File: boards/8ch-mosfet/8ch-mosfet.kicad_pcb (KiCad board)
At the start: 2 copper layers, 184.5 x 137 mm, 153 parts, among them J1 N2K, J10 Screw_Terminal_01x02, J11 Screw_Terminal_01x02, J12 Screw_Terminal_01x02, J2 I2C, J3 Screw_Terminal_01x08, J5 Screw_Terminal_01x02, J6 Screw_Terminal_01x02, J7 Screw_Terminal_01x02, J8 Screw_Terminal_01x02, J9 Screw_Terminal_01x02, M1 Fan_4pin, M2 Fan_4pin, Q1 2N7002, Q10 IRF4905, Q11 2N7002, Q12 IRF4905, Q13 2N7002, Q14 IRF4905, Q15 2N7002, Q16 IRF4905, Q2 IRF4905, Q3 2N7002, Q4 IRF4905, Q5 2N7002, Q6 IRF4905, Q7 2N7002, Q8 IRF4905, Q9 2N7002, U1 ESP32-DEVKITC, U10 ACS725xLCTR-20AU, U11 ACS725xLCTR-20AU, U12 ACS725xLCTR-20AU, U13 MCP1502, U2 MCP3208, U3 R-78K5.0-1.0, U4 MCP3221A0T, U5 ACS725xLCTR-20AU, U6 ACS725xLCTR-20AU, U7 ACS725xLCTR-20AU, U8 ACS725xLCTR-20AU, U9 ACS725xLCTR-20AU

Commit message: more routing and layout
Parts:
- removed J1: N2K, Connector_PinHeader_2.54mm:PinHeader_1x04_P2.54mm_Vertical
- removed J2: I2C, Connector_PinHeader_2.54mm:PinHeader_1x04_P2.54mm_Vertical
- removed R40: 2.2K, Resistor_SMD:R_0805_2012Metric_Pad1.20x1.40mm_HandSolder
- added C31: 33pF, Capacitor_SMD:C_0805_2012Metric_Pad1.18x1.45mm_HandSolder, F.Cu at (-56.4, -0.26)
- added C32: 33pF, Capacitor_SMD:C_0805_2012Metric_Pad1.18x1.45mm_HandSolder, F.Cu at (-63.3, -0.26)
- added C33: 33pF, Capacitor_SMD:C_0805_2012Metric_Pad1.18x1.45mm_HandSolder, F.Cu at (-56.4, 4.32)
- added C34: 33pF, Capacitor_SMD:C_0805_2012Metric_Pad1.18x1.45mm_HandSolder, F.Cu at (-63.2, 4.32)
- added C35: 10uF, Capacitor_SMD:C_0805_2012Metric_Pad1.18x1.45mm_HandSolder, F.Cu at (-56.4, 8.91)
- added C36: 10uF, Capacitor_SMD:C_0805_2012Metric_Pad1.18x1.45mm_HandSolder, F.Cu at (-54.1, 8.89)
- added C37: 33pF, Capacitor_SMD:C_0805_2012Metric_Pad1.18x1.45mm_HandSolder, F.Cu at (-16.6, 7.17)
- added C38: 33pF, Capacitor_SMD:C_0805_2012Metric_Pad1.18x1.45mm_HandSolder, F.Cu at (-16.6, 10.2)
- added C39: 10uF, Capacitor_SMD:C_0805_2012Metric_Pad1.18x1.45mm_HandSolder, F.Cu at (-21.6, 26.4)
- added C40: 33pF, Capacitor_SMD:C_0805_2012Metric_Pad1.18x1.45mm_HandSolder, F.Cu at (-11.8, 4.32)
- added C41: 33pF, Capacitor_SMD:C_0805_2012Metric_Pad1.18x1.45mm_HandSolder, F.Cu at (-11.8, 7.17)
- added C42: 10uF, Capacitor_SMD:C_0805_2012Metric_Pad1.18x1.45mm_HandSolder, F.Cu at (-11.2, -0.76)
- added C43: 1uF/50v, Capacitor_SMD:C_0805_2012Metric_Pad1.18x1.45mm_HandSolder, F.Cu at (-46.8, 39.9)
- added C44: 4.7uF/50v, Capacitor_SMD:C_0805_2012Metric_Pad1.18x1.45mm_HandSolder, F.Cu at (-46.8, 42.9)
- added C45: 22uF/35v, Capacitor_SMD:C_0805_2012Metric_Pad1.18x1.45mm_HandSolder, F.Cu at (-46.8, 45.9)
- added C46: 22nF, Capacitor_SMD:C_0805_2012Metric_Pad1.18x1.45mm_HandSolder, F.Cu at (-46.8, 48.9)
- added C47: 47uF/6.3v, Capacitor_SMD:C_0805_2012Metric_Pad1.18x1.45mm_HandSolder, F.Cu at (-46.8, 51.9)
- added D1: PESD5V0L1BA, Diode_SMD:D_SOD-323_HandSoldering, F.Cu at (-58.7, -0.26)
- added D27: PESD5V0L1BA, Diode_SMD:D_SOD-323_HandSoldering, F.Cu at (-58.7, 4.32)
- added D28: PESD5V0L1BA, Diode_SMD:D_SOD-323_HandSoldering, F.Cu at (-58.7, 8.89)
- added D29: PESD5V0L1BA, Diode_SMD:D_SOD-323_HandSoldering, F.Cu at (-28.4, 21.8)
- added D30: PESD5V0L1BA, Diode_SMD:D_SOD-323_HandSoldering, F.Cu at (-28.4, 27.4)
- added D31: PESD5V0L1BA, Diode_SMD:D_SOD-323_HandSoldering, F.Cu at (-22.9, 23.1)
- added D32: PESD5V0L1BA, Diode_SMD:D_SOD-323_HandSoldering, F.Cu at (-36.1, 50.5)
- added D33: DSK24, Diode_SMD:D_SOD-123, F.Cu at (-41.5, 50.7)
- added F9: MD050-60V, Fuse:Fuse_1812_4532Metric_Pad1.30x3.40mm_HandSolder, F.Cu at (-40.8, 46.6)
- added FB1: GZ2012D601TF, Inductor_SMD:L_0805_2012Metric, F.Cu at (-61.0, -0.27)
- added FB2: GZ2012D601TF, Inductor_SMD:L_0805_2012Metric, F.Cu at (-61.0, 4.32)
- added FB3: GZ2012D601TF, Inductor_SMD:L_0805_2012Metric, F.Cu at (-61.0, 8.89)
- added FB4: GZ2012D601TF, Inductor_SMD:L_0805_2012Metric, F.Cu at (-26.1, 9.27)
- added FB5: GZ2012D601TF, Inductor_SMD:L_0805_2012Metric, F.Cu at (-22.9, 17.5)
- added FB6: GZ2012D601TF, Inductor_SMD:L_0805_2012Metric, F.Cu at (-23.1, 20.3)
- added FB7: GZ2012D601TF, Inductor_SMD:L_0805_2012Metric, F.Cu at (-35.4, 39.8)
- added J13: I2C, Connector_PinHeader_2.54mm:PinHeader_1x04_P2.54mm_Vertical, F.Cu at (-50.8, 0.52)
- added J14: N2K, Connector_PinHeader_2.54mm:PinHeader_1x04_P2.54mm_Vertical, F.Cu at (-16.9, 14.0)
- added L2: SMMS0650-470M, Inductor_SMD:L_Chilisin_BMRA00040420, F.Cu at (-41.1, 41.3)
- added R42: 2.2k, Resistor_SMD:R_0805_2012Metric_Pad1.20x1.40mm_HandSolder, F.Cu at (-54.1, -0.27)
- added R43: 2.2k, Resistor_SMD:R_0805_2012Metric_Pad1.20x1.40mm_HandSolder, F.Cu at (-54.1, 4.32)
- C1: value 10uF -> 470nF/50v
- C2: value 10uF -> 10nF/50v
- L1: value 100uH -> CBC3225T100KR; footprint Inductor_SMD:L_1210_3225Metric_Pad1.42x2.65mm_HandSolder -> Inductor_SMD:L_1210_3225Metric
- R39: value 2.2K -> 4.7R
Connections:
- net Net-(D26-K) renamed ESP32_VIN
- C1 pad 1: +24V -> Net-(D32-A2)
- C2 pad 1: Net-(U3-IN) -> Net-(D32-A2)
- C27 pad 2: +5V -> Net-(D33-K)
- L1 pad 1: +24V -> Net-(D32-A2)
- R39 pad 1: SDA -> Net-(C44-Pad2)
- R39 pad 2: +3.3V -> GNDD
- U3 pad 3: +5V -> Net-(D33-K)
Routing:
- net GNDD: track 23.5 -> 54.1 mm
- net +3.3V: track 266.9 -> 291.9 mm
- net Net-(D1-A2): track 0.00 -> 9.85 mm
- net Net-(D27-A2): track 0.00 -> 8.76 mm
- net Net-(D28-A2): track 0.00 -> 7.09 mm
- net SDA: track 50.7 -> 55.1 mm
- net SCL: track 42.0 -> 46.1 mm

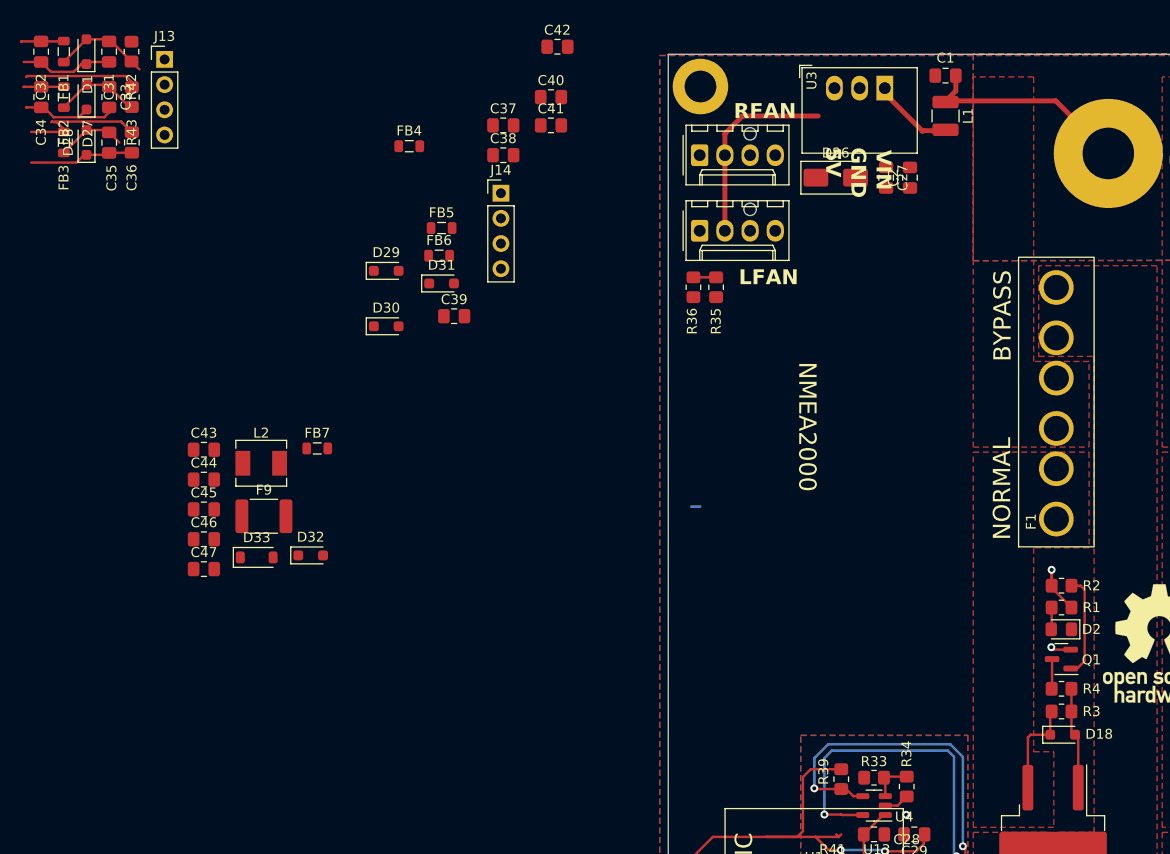
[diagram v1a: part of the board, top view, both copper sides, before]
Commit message: more or less placed all the stuff that needs to be placed
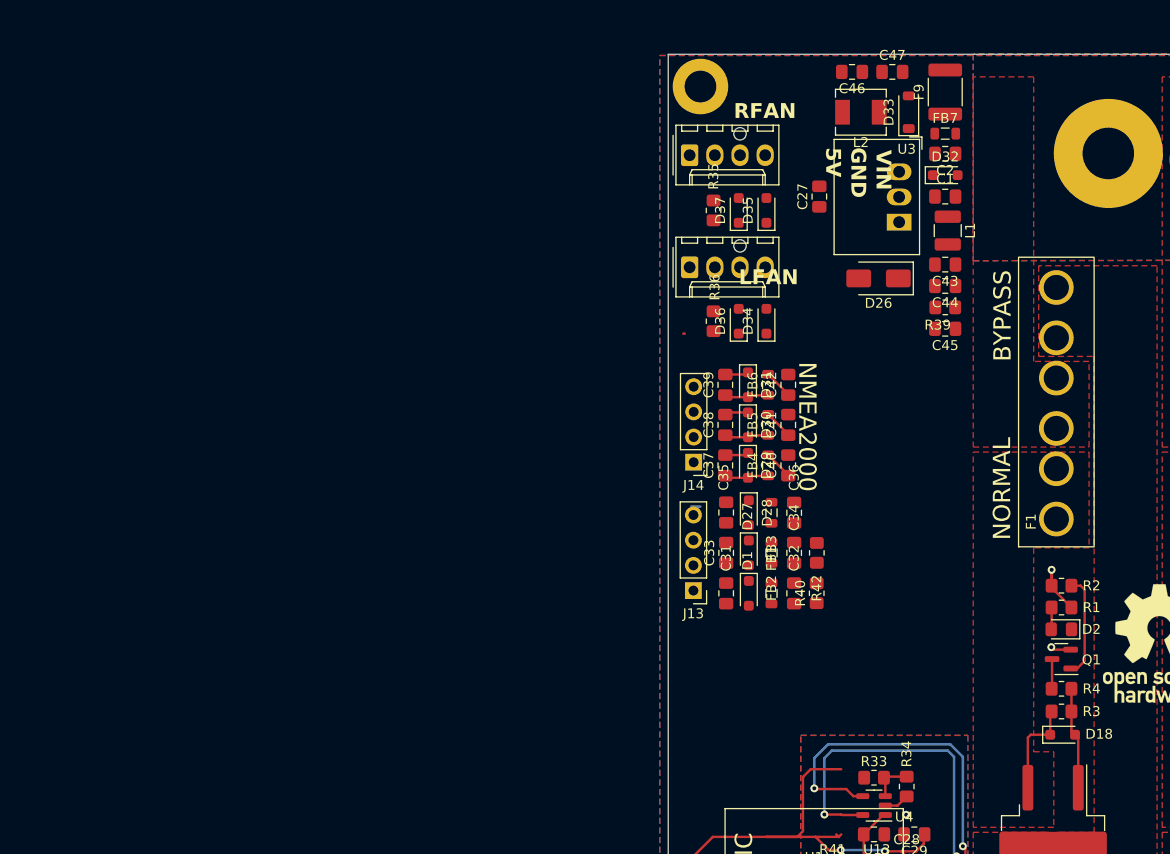
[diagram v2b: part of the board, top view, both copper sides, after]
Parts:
- removed R43: 2.2k, Resistor_SMD:R_0805_2012Metric_Pad1.20x1.40mm_HandSolder
- added D34: PESD5V0L1BA, Diode_SMD:D_SOD-323_HandSoldering, F.Cu at (9.91, 26.9)
- added D35: PESD5V0L1BA, Diode_SMD:D_SOD-323_HandSoldering, F.Cu at (9.91, 15.7)
- added D36: PESD5V0L1BA, Diode_SMD:D_SOD-323_HandSoldering, F.Cu at (7.11, 26.9)
- added D37: PESD5V0L1BA, Diode_SMD:D_SOD-323_HandSoldering, F.Cu at (7.11, 15.7)
- added R40: 2.2k, Resistor_SMD:R_0805_2012Metric_Pad1.20x1.40mm_HandSolder, F.Cu at (15.0, 54.4)
- moved C32 93.6 mm to (12.7, 54.4), turned to 90 degrees
- moved FB1 89.9 mm to (10.4, 54.4), turned to -90 degrees
- moved C34 88.8 mm to (12.7, 50.3), turned to 90 degrees
- moved D1 86.3 mm to (8.13, 54.4), turned to -90 degrees
- moved C47 85.7 mm to (22.6, 1.78)
- moved R42 85.6 mm to (15.0, 50.3)
- moved FB2 84.9 mm to (10.4, 50.3)
- moved C31 82.8 mm to (5.84, 54.4), turned to 90 degrees
- moved D27 81.1 mm to (8.13, 50.3), turned to -90 degrees
- moved F9 81.0 mm to (27.9, 3.81), turned to 90 degrees
- moved C46 80.6 mm to (18.5, 1.78), turned to 180 degrees
- moved FB3 80.6 mm to (10.4, 46.2)
- moved D33 79.6 mm to (24.3, 5.84), turned to 90 degrees
- moved C33 77.4 mm to (5.84, 50.3), turned to 90 degrees
- moved C44 77.3 mm to (27.9, 23.4), turned to 180 degrees
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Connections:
- R42 pad 1: Net-(D1-A2) -> SCL
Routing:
- net +3.3V: track 291.9 -> 267.6 mm
- net GNDD: track 54.1 -> 30.6 mm
- net +24V: track 21.6 -> 0.00 mm
- net +5V: track 19.9 -> 0.00 mm
- net Net-(D1-A2): track 9.85 -> 0.00 mm
- net Net-(D27-A2): track 8.76 -> 0.00 mm
- net Net-(U3-IN): track 8.30 -> 0.00 mm
- net Net-(D28-A2): track 7.09 -> 0.92 mm
- net Net-(D31-A2): track 0.00 -> 4.48 mm
- net Net-(D29-A2): track 0.00 -> 4.48 mm
- net Net-(D30-A2): track 0.00 -> 4.48 mm
- net SDA: track 55.1 -> 50.7 mm
- net SCL: track 46.1 -> 42.0 mm
- net CAN_TX: track 40.6 -> 43.5 mm
- net CAN_RX: track 38.2 -> 41.2 mm
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
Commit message: whew, lots of routing.
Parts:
- added REF**: MountingHole_3.2mm_M3_DIN965_Pad, MountingHole:MountingHole_3.2mm_M3_DIN965_Pad, F.Cu at (14.0, 133.0)
- moved REF** 53.8 mm to (3.00, 80.0)
- moved R37 29.1 mm to (21.3, 103.9), turned to 180 degrees
- moved U1 7.00 mm to (2.00, 90.1)
- moved U13 3.23 mm to (22.7, 85.4)
- moved R34 3.04 mm to (25.9, 76.3)
- moved C28 2.70 mm to (22.0, 81.1)
- moved R33 2.70 mm to (22.0, 75.4)
- moved U4 2.70 mm to (22.0, 78.2)
- moved R41 2.54 mm to (18.0, 83.9)
- moved C30 2.44 mm to (18.0, 86.1)
- moved R38 1.84 mm to (21.3, 101.3), turned to 0 degrees
- moved C29 1.81 mm to (25.9, 80.1), turned to -90 degrees
- moved D35 0.51 mm to (9.91, 16.3)
- moved D37 0.51 mm to (7.11, 16.3)
- moved M1 0.51 mm to (2.16, 10.7)
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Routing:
- net /PWM7: track 69.4 -> 239.1 mm, vias 1 -> 2
- net /PWM5: track 25.9 -> 193.7 mm, vias 1 -> 2
- net /PWM6: track 56.2 -> 215.4 mm, vias 1 -> 2
- net /PWM4: track 44.8 -> 173.0 mm, vias 1 -> 2
- net /PWM3: track 37.9 -> 152.2 mm, vias 1 -> 2
- net FAN_PWM2: track 40.9 -> 140.8 mm
- net /PWM2: track 33.3 -> 131.2 mm, vias 1 -> 2
- net FAN_TACH2: track 7.73 -> 101.1 mm
- net FAN_TACH1: track 3.05 -> 92.6 mm
- net /PWM1: track 24.0 -> 109.9 mm, vias 1 -> 2
- net FAN_PWM1: track 36.4 -> 110.5 mm
- net ESP32_VIN: track 48.9 -> 122.8 mm
- net /PWM0: track 17.6 -> 88.9 mm, vias 1 -> 2
- net CAN_RX: track 41.2 -> 99.9 mm
- net +24V: track 0.00 -> 53.8 mm
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
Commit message: finished the massive re-route
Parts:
- moved C36 1.28 mm to (13.5, 45.2), turned to 0 degrees
- turned C32 to -90 degrees
- turned C40 to -90 degrees
- turned R40 to -90 degrees
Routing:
- net +3.3V: track 295.1 -> 359.2 mm
- net +5V: track 0.00 -> 53.8 mm, vias 0 -> 1
- net SCL: track 28.3 -> 74.9 mm, vias 2 -> 4
- net SDA: track 39.3 -> 82.1 mm, vias 2 -> 4
- net Net-(U3-IN): track 0.00 -> 24.8 mm
- net +24V: track 53.8 -> 73.8 mm
- net Net-(D33-K): track 0.00 -> 17.1 mm
- net FAN_PWM1: track 110.5 -> 124.8 mm, vias 0 -> 2
- net FAN_TACH2: track 101.1 -> 112.0 mm
- net CAN_TX: track 95.6 -> 106.2 mm, vias 1 -> 3
- net Net-(D1-A2): track 0.00 -> 9.47 mm
- net Net-(D32-A2): track 0.00 -> 8.89 mm
- net Net-(D28-A2): track 0.92 -> 9.30 mm
- net Net-(D27-A2): track 0.00 -> 8.13 mm
- net CAN_RX: track 99.9 -> 107.7 mm, vias 0 -> 2
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
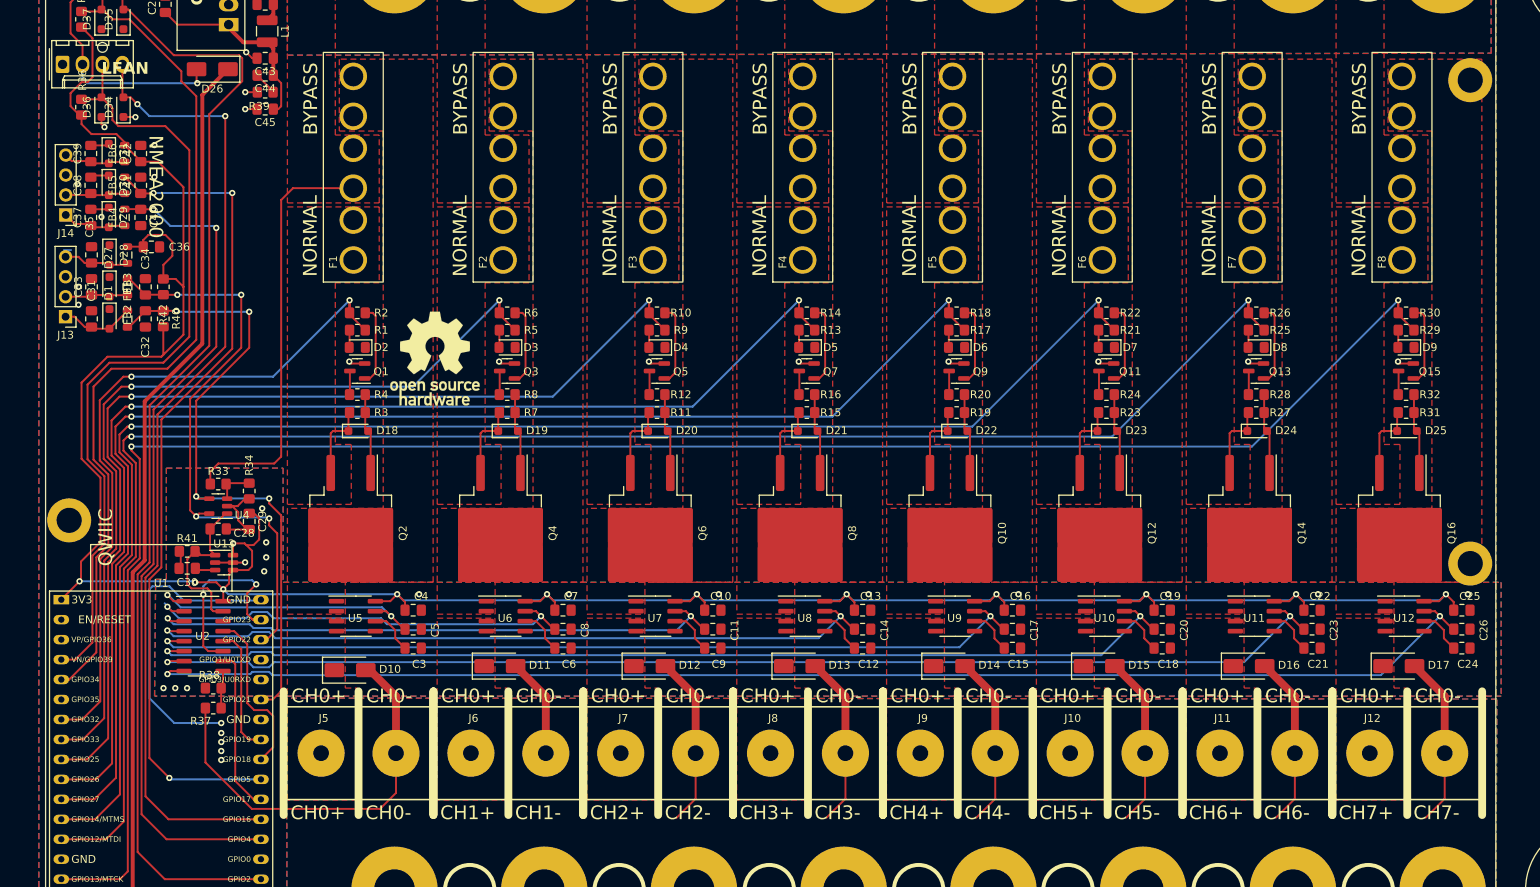
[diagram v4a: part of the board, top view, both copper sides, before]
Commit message: fixed drc errors, just silkscreen left
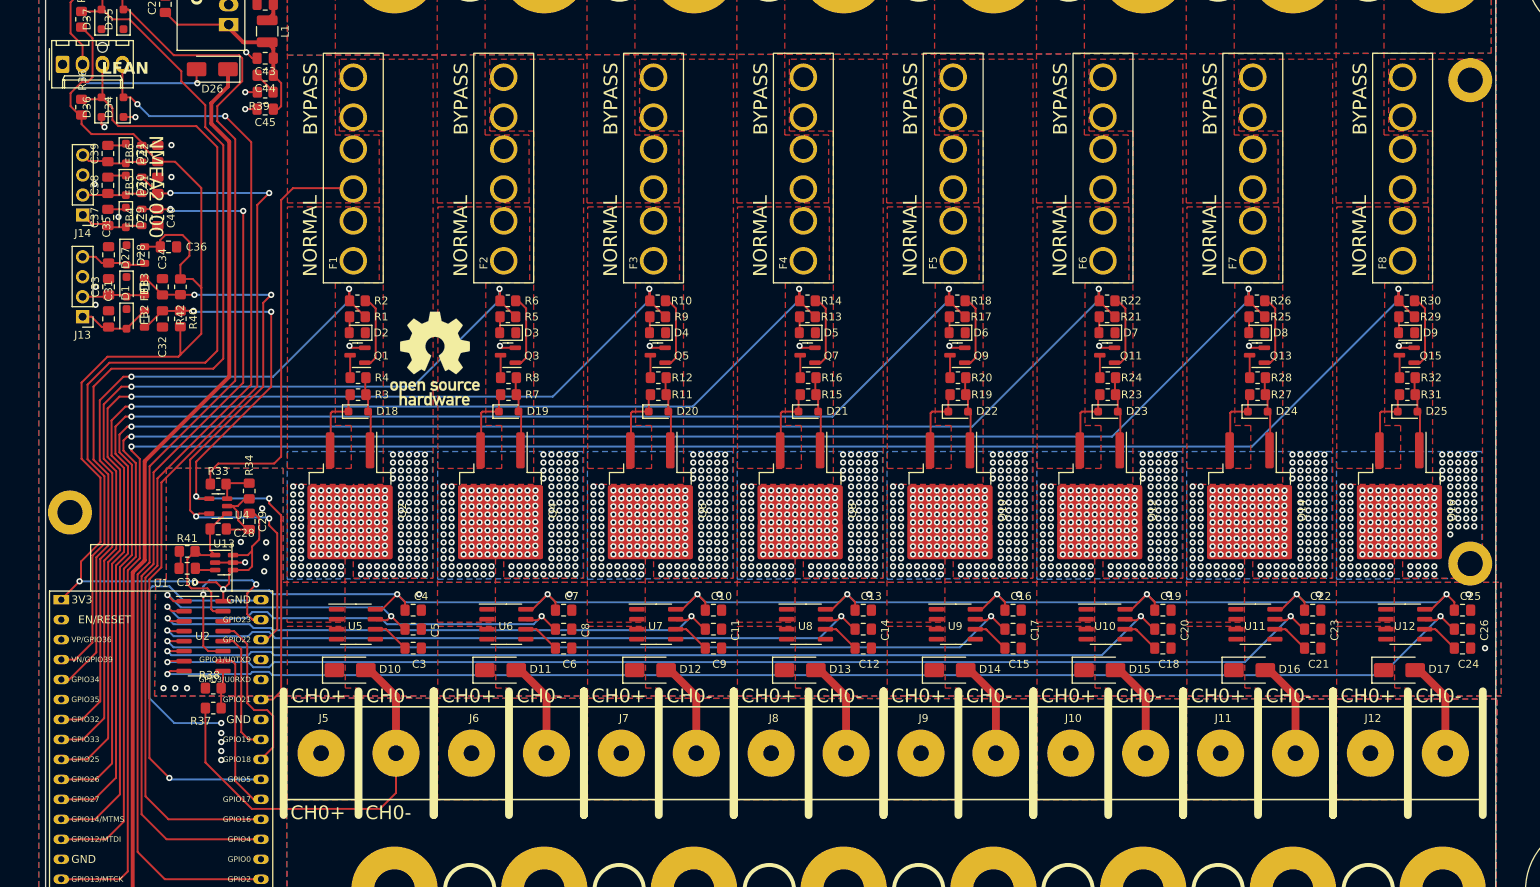
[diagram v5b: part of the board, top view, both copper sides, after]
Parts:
- moved Q2 2.89 mm to (38.7, 78.7)
- moved Q10 2.88 mm to (115.1, 78.7)
- moved Q12 2.88 mm to (134.1, 78.7)
- moved Q14 2.88 mm to (153.2, 78.7)
- moved Q16 2.88 mm to (172.2, 78.7)
- moved Q4 2.88 mm to (57.9, 78.7)
- moved Q6 2.88 mm to (76.9, 78.7)
- moved Q8 2.88 mm to (96.0, 78.7)
- moved D23 2.47 mm to (135.2, 66.2)
- moved D24 2.47 mm to (154.2, 66.2)
- moved D25 2.47 mm to (173.3, 66.2)
- moved D19 2.47 mm to (58.9, 66.2)
- moved D20 2.47 mm to (78.0, 66.2)
- moved D21 2.47 mm to (97.0, 66.2)
- moved D22 2.47 mm to (116.1, 66.2)
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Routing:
- net GNDPWR: track 196.0 -> 139.2 mm
- net FAN_TACH1: track 100.1 -> 108.5 mm
- net +3.3V: track 359.2 -> 366.8 mm, vias 12 -> 11
- net FAN_TACH2: track 112.0 -> 118.3 mm
- net CAN_TX: track 106.2 -> 110.7 mm
- net CAN_RX: track 107.7 -> 111.7 mm
- net SCL: track 74.9 -> 78.1 mm
- net FAN_PWM1: track 124.8 -> 127.6 mm
- net /PWM4: track 173.0 -> 175.6 mm
- net /PWM7: track 239.1 -> 241.7 mm
- net /PWM6: track 215.4 -> 218.0 mm
- net /PWM3: track 152.2 -> 154.9 mm
- net /PWM2: track 131.2 -> 133.8 mm
- net /PWM1: track 109.9 -> 112.5 mm
- net /PWM5: track 193.7 -> 196.4 mm
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- added copper zone on B.Cu, net Net-(Q10-D)
- added copper zone on B.Cu, net Net-(Q12-D)
- added copper zone on B.Cu, net Net-(Q14-D)
- added copper zone on B.Cu, net Net-(Q16-D)
- added copper zone on B.Cu, net Net-(Q2-D)
- added copper zone on B.Cu, net Net-(Q4-D)
- added copper zone on B.Cu, net Net-(Q6-D)
- added copper zone on B.Cu, net Net-(Q8-D)
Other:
- board text removed: "CH1+"
- board text removed: "CH1-"
- board text removed: "CH2+"
- board text removed: "CH2-"
- board text removed: "CH3+"
- board text removed: "CH3-"
- board text removed: "CH4+"
- board text removed: "CH4-"
- board text removed: "CH5+"
- board text removed: "CH5-"
- board text removed: "CH6+"
- board text removed: "CH6-"
- board text removed: "CH7+"
- board text removed: "CH7-"
- board text removed: "QWIIC"
